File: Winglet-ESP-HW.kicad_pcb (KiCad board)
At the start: 2 copper layers, 30 x 47.6 mm, 37 parts, among them M1 Mount_M2.5, M2 Mount_M2.5, Q1 DMG1013UW-7, Q2 DMG1012UW-7, Q3 DMG1012UW-7, U1 24AA01T-I/OT, U2 ESP32-C3-MINI-1U-N4, U3 TC1262-3.0VDBTR, U4 FXLA108BQX, Y1 SC32S-7PF20PPM

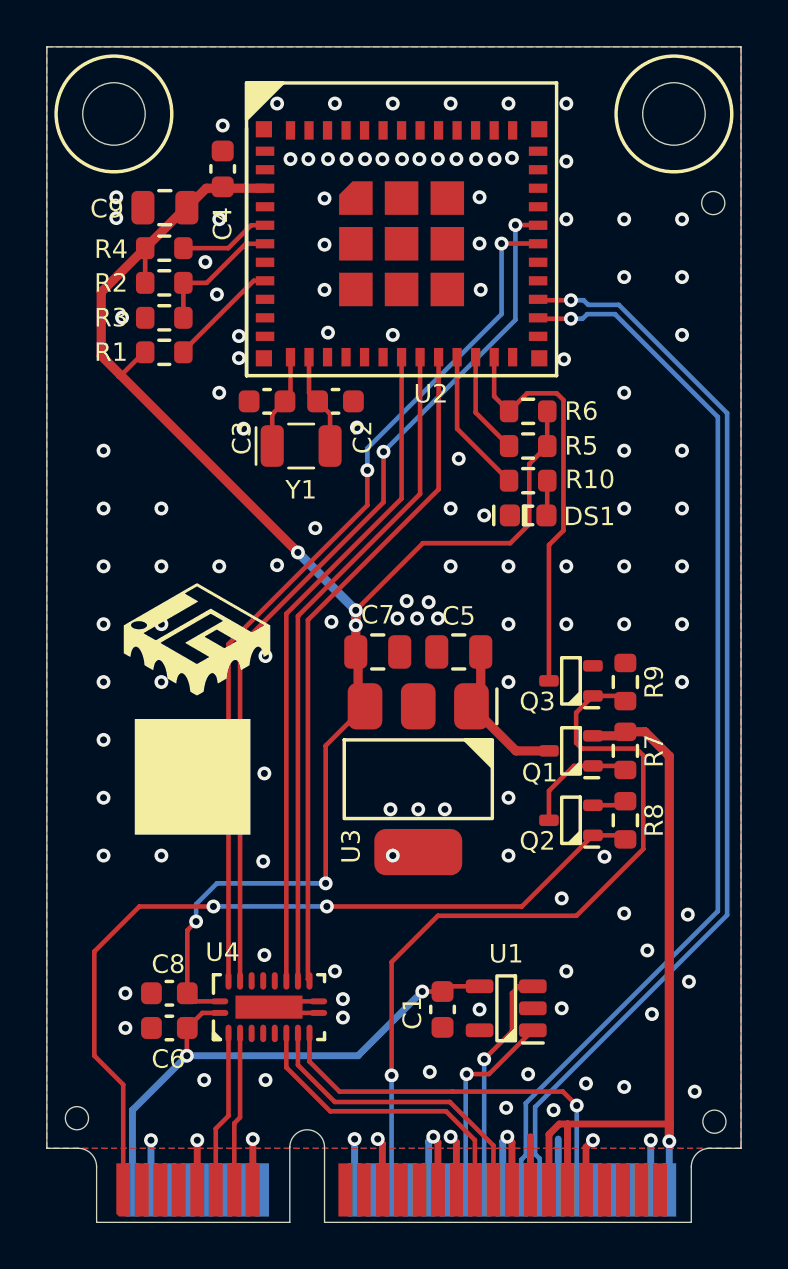
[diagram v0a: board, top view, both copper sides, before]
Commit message: Overhaul for buck-boost converter
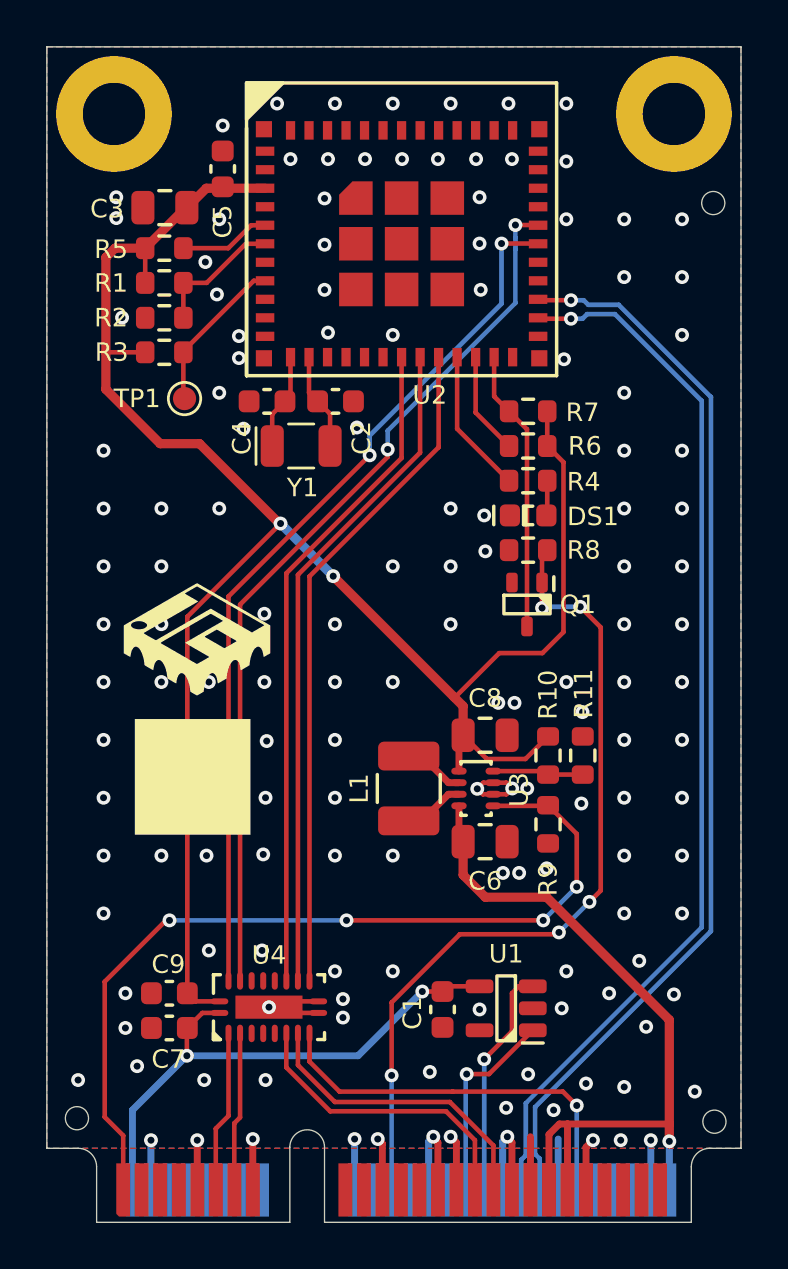
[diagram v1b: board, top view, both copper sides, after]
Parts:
- removed the C5 at (102.8, 78.5)
- removed the C7 at (99.3, 78.5)
- removed the Q1 at (107.7, 82.8)
- removed Q2: DMG1012UW-7, U_IC:SC70-3
- removed the R7 at (110.0, 82.8)
- added C6: 10u, C_Capacitor:C_0805, F.Cu at (103.9, 86.8)
- added C8: 47u,6.3V, C_Capacitor:C_0805, F.Cu at (103.9, 82.2)
- added L1: NLCV32T-1R0M-PFR, L_Inductor:L_1210, F.Cu at (100.6, 84.5)
- added R10: 560K, R_Resistor:R_0603, F.Cu at (106.7, 83.0)
- added R11: 100K, R_Resistor:R_0603, F.Cu at (108.2, 83.0)
- added TP1: ~, TP_TestPoint:TestPoint_1mm, F.Cu at (91.0, 67.6)
- M1, M2: value Mount_M2.5 -> PTH_M2.5; footprint M_Mechanical:Mount_M2.5 -> M_Mechanical:PTH_M2.5
- U3: value TC1262-3.0VDBTR -> TPS631000DRLR; footprint U_IC:SOT223_3 -> U_IC:SOT583
- moved M1 24.2 mm to (87.9, 55.3), turned to 90 degrees
- moved M2 24.2 mm to (112.1, 55.3), turned to 90 degrees
- moved R8 7.08 mm to (105.8, 74.2), turned to 180 degrees
- moved Q1 3.81 mm to (105.8, 76.5), turned to -90 degrees
- moved R9 3.34 mm to (106.7, 86.0), turned to -90 degrees
- moved U3 2.53 mm to (103.5, 84.5), turned to 0 degrees
- renumbered C9 to C3, C3 to C4, C4 to C5, C6 to C7, C8 to C9, Q3 to Q1, R2 to R1, R3 to R2, R1 to R3, R10 to R4, R4 to R5, R5 to R6, R6 to R7, R9 to R8, R8 to R9
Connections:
- net Net-(U2-EN) renamed /ESP/ESP_EN
- U3 pad 1: Net-(Q1-D) -> +VDD
- U3 pad 2: GND -> Net-(U3-LX2)
- U3 pad 3: +VDD -> Net-(U3-LX1)
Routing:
- net +VDD: track 69.3 -> 84.7 mm, vias 5 -> 2
- net Net-(Q1-D): track 6.66 -> 0.00 mm
- net /ESP/ESP_BOOT: track 17.8 -> 12.2 mm
- net Net-(Q1-G): track 5.09 -> 0.00 mm
- net Net-(U3-FB): track 0.00 -> 3.93 mm
- net Net-(U3-LX2): track 0.00 -> 2.65 mm
- net Net-(U3-LX1): track 0.00 -> 2.65 mm
- net /Connector/RESET: track 33.7 -> 36.0 mm, vias 1 -> 5
- net /ESP/ESP_EN: track 4.79 -> 6.81 mm
- net GND: track 37.8 -> 39.8 mm, vias 134 -> 148
- net /Connector/WAKE: track 35.9 -> 37.8 mm, vias 2 -> 4
- net +BATT: track 33.2 -> 32.6 mm
- net /Connector/USB_DP: track 47.3 -> 46.7 mm
- net /Connector/USB_DM: track 46.6 -> 46.1 mm
